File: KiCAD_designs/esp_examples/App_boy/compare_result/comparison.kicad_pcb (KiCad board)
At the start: 2 copper layers, 57 x 72 mm, 26 parts, among them J1 B4B-ZR-SM4-TFT_LF__SN_, J2 B2B-PH-SM4-TBLFSN, J3 Conn_01x02_Pin, J4 B4B-ZR-SM4-TFT_LF__SN_, J5 Conn_01x02_Pin, J6 B7B-ZR-SM4-TFT_LF__SN_, SW2 RS-282G05A3-SM RT, SW3 RS-282G05A3-SM RT, U1 ESP-12F, U2 AMS1117-3.3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

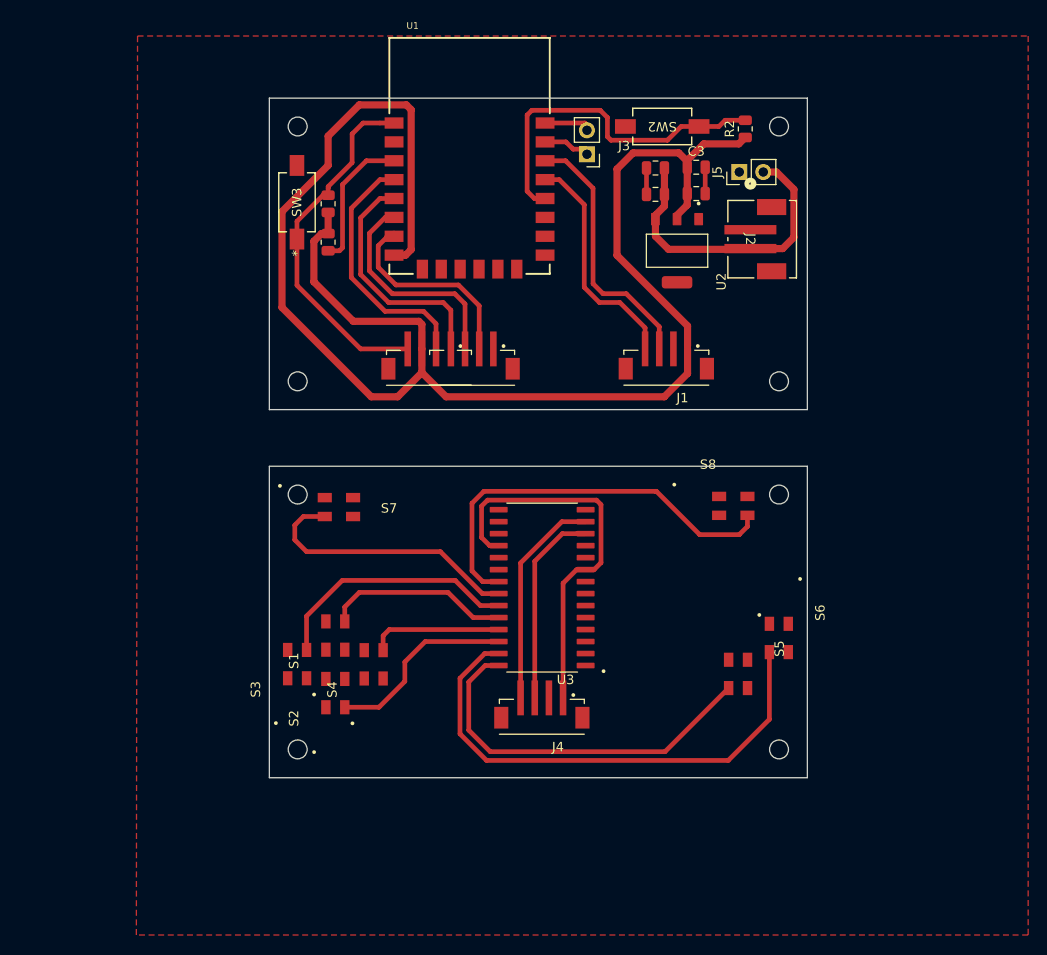
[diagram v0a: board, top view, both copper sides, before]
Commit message: UI mistake cam_roller
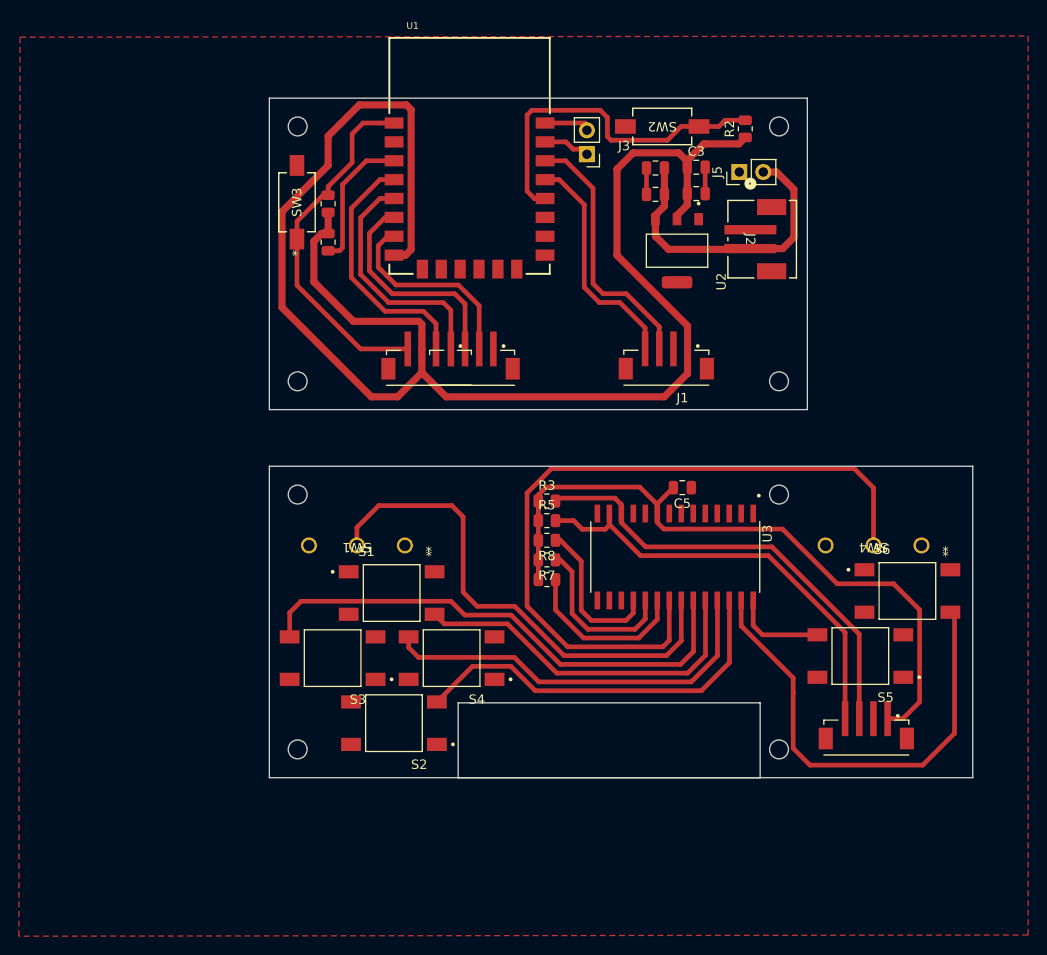
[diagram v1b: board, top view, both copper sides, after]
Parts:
- removed S7: RL, esp_lib:switch
- removed S8: RR, esp_lib:switch
- added C5: C, Capacitor_SMD:C_0805_2012Metric, F.Cu at (83.8, 66.3)
- added R3: R, Resistor_SMD:R_0805_2012Metric, F.Cu at (69.4, 67.7)
- added R5: R, Resistor_SMD:R_0805_2012Metric, F.Cu at (69.4, 69.8)
- added R6: R, Resistor_SMD:R_0805_2012Metric, F.Cu at (69.4, 76.0)
- added R7: R, Resistor_SMD:R_0805_2012Metric, F.Cu at (69.4, 73.9)
- added R8: R, Resistor_SMD:R_0805_2012Metric, F.Cu at (69.4, 71.8)
- added SW1: D2FS-FL-N-A, esp_lib:D2FS-FL-N-A_OMR, F.Cu at (54.4, 72.4)
- added SW4: D2FS-FL-N-A, esp_lib:D2FS-FL-N-A_OMR, F.Cu at (109.1, 72.4)
- S1, S2, S3, S4, S5, S6: footprint esp_lib:switch -> esp_lib:switch_6
- moved J4 34.5 mm to (103.3, 92.7)
- moved S6 14.5 mm to (107.6, 77.2), turned to 0 degrees
- moved U3 14.5 mm to (83.0, 73.6), turned to -90 degrees
- moved S5 13.1 mm to (102.6, 84.1), turned to 180 degrees
- moved S4 8.28 mm to (59.3, 84.3), turned to 180 degrees
- moved S1 7.48 mm to (53.0, 77.4), turned to 0 degrees
- moved S2 6.98 mm to (53.2, 91.2), turned to 180 degrees
- moved S3 3.81 mm to (46.7, 84.3), turned to 180 degrees
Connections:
- U3 pad 15: unconnected-(U3-A0-Pad15) -> GND
- U3 pad 16: unconnected-(U3-A1-Pad16) -> GND
- U3 pad 17: unconnected-(U3-A2-Pad17) -> GND
- U3 pad 18: VCC -> Net-(U3-~{RESET})
- U3 pad 19: unconnected-(U3-INTB-Pad19) -> Net-(U3-INTB)
- U3 pad 20: unconnected-(U3-INTA-Pad20) -> Net-(U3-INTA)
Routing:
- net /RR: track 43.6 -> 78.1 mm
- net VCC: track 213.8 -> 245.5 mm
- net /A: track 40.3 -> 9.86 mm
- net /right: track 14.0 -> 41.6 mm
- net /left: track 26.6 -> 53.9 mm
- net /SCK_mcp: track 49.6 -> 76.0 mm
- net /SDA_mcp: track 47.8 -> 72.3 mm
- net /RL: track 29.1 -> 53.4 mm
- net /down: track 20.4 -> 40.7 mm
- net Net-(U3-INTA): track 0.00 -> 18.1 mm
- net /up: track 19.6 -> 37.2 mm
- net Net-(U3-INTB): track 0.00 -> 17.6 mm
- net Net-(U3-~{RESET}): track 0.00 -> 16.5 mm
- net /B: track 53.9 -> 50.1 mm
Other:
- board size 57 x 72 mm -> 74.5 x 72 mm
